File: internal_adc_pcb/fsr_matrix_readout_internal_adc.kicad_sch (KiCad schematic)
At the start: 2 parts

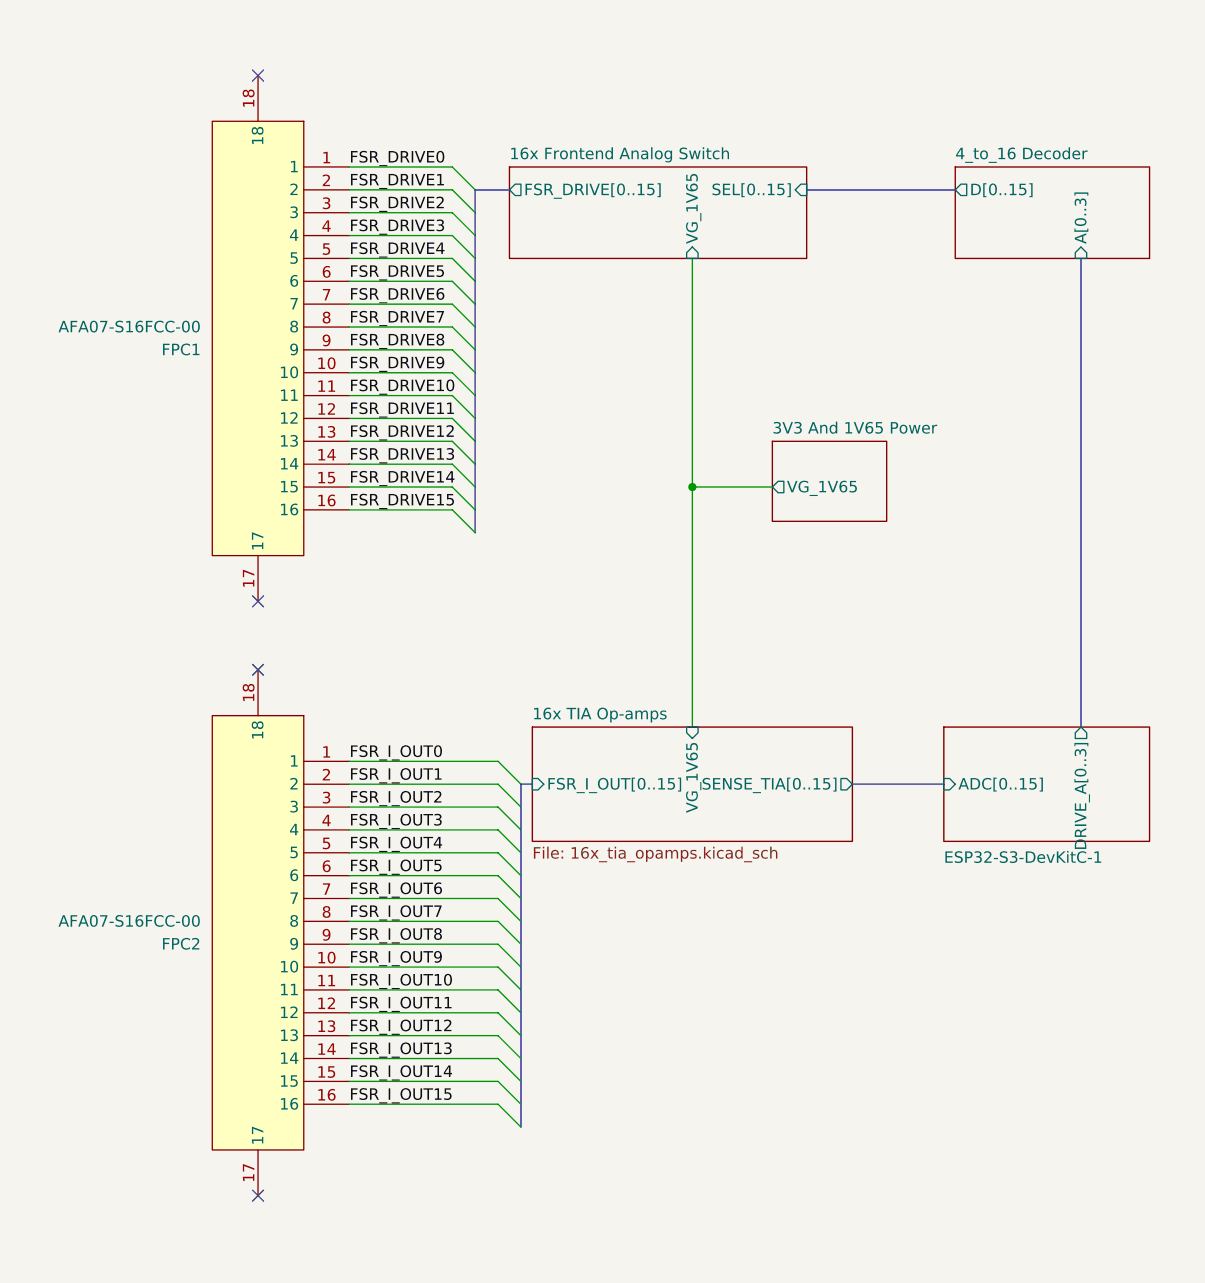
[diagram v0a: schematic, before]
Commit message: adjust VG issue for internal ADC version; changed naming for VG
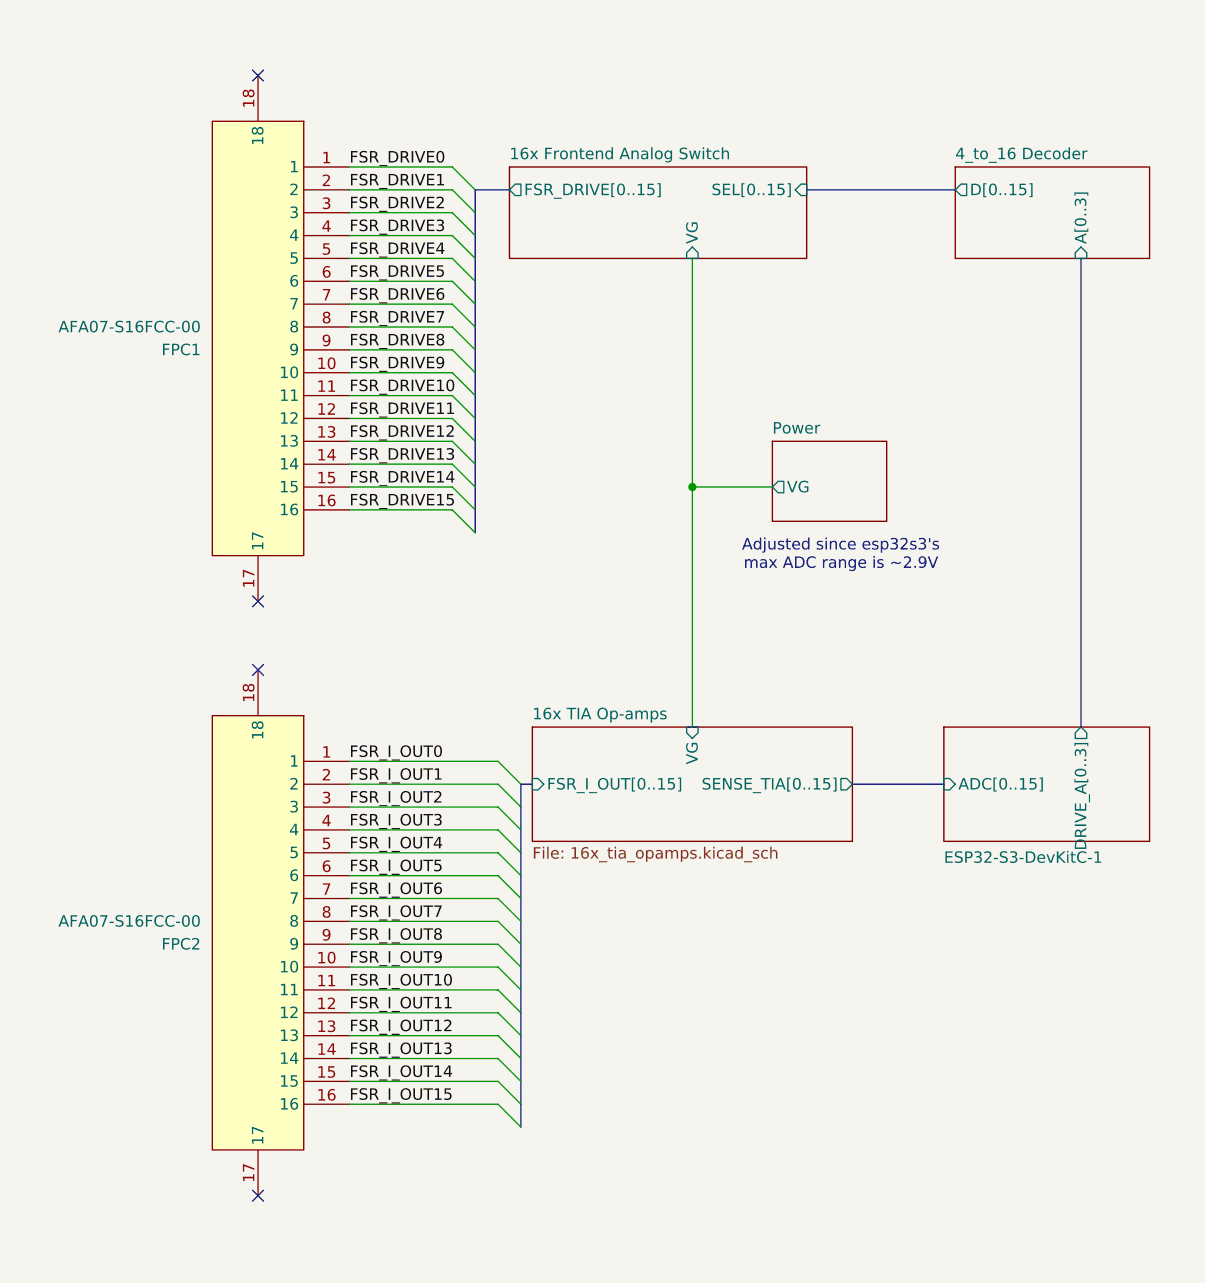
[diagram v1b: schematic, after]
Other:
- sheet 3V3 And 1V65 Power renamed Power
- sheet 16x Frontend Analog Switch ports: added VG; removed VG_1V65
- sheet 16x TIA Op-amps ports: added VG; removed VG_1V65
- sheet Power: file 3V3 And 1V65 Power.kicad_sch -> power.kicad_sch
- sheet Power ports: added VG; removed VG_1V65
- note added: "Adjusted since esp32s3's max ADC range is ~2.9V"
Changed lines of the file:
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@@
 	(generator_version "10.0")
 	(paper "A4")
+	(text "Adjusted since esp32s3's \nmax ADC range is ~2.9V"
+		(exclude_from_sim no)
+		(at 121.92 93.98 0)
+		(effects
+			(font
+				(size 1.27 1.27)
+			)
+		)
+	)
 	(junction
 		(at 105.41 86.36)
@@
 		(members "7bcd2658-0b6a-4321-9860-384b8d346995")
 	)
-	(group "3V3 And 1V65 Power"
-		(lib_id "FSR_readout:3V3 And 1V65 Power")
+	(group "Power"
+		(lib_id "FSR_readout:Power")
 		(members "fdc75ebc-7ada-4013-b8f9-952e82a3d457")
 	)
@@
 			)
 		)
-		(pin "VG_1V65" input
+		(pin "VG" input
 			(at 105.41 60.96 270)
 			(effects
@@
 			)
 		)
-		(pin "VG_1V65" input
+		(pin "VG" input
 			(at 105.41 113.03 90)
 			(effects
@@
 			(color 0 0 0 0)
 		)
-		(property "Sheetname" "3V3 And 1V65 Power"
+		(property "Sheetname" "Power"
 			(at 114.3 80.5684 0)
 			(show_name no)
@@
 			)
 		)
-		(property "Sheetfile" "3V3 And 1V65 Power.kicad_sch"
+		(property "Sheetfile" "power.kicad_sch"
 			(at 114.3 90.7546 0)
 			(hide yes)
@@
 			)
 		)
-		(pin "VG_1V65" output
+		(pin "VG" output
 			(at 114.3 86.36 180)
 			(effects

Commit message: add testpoint for internal ADC ver
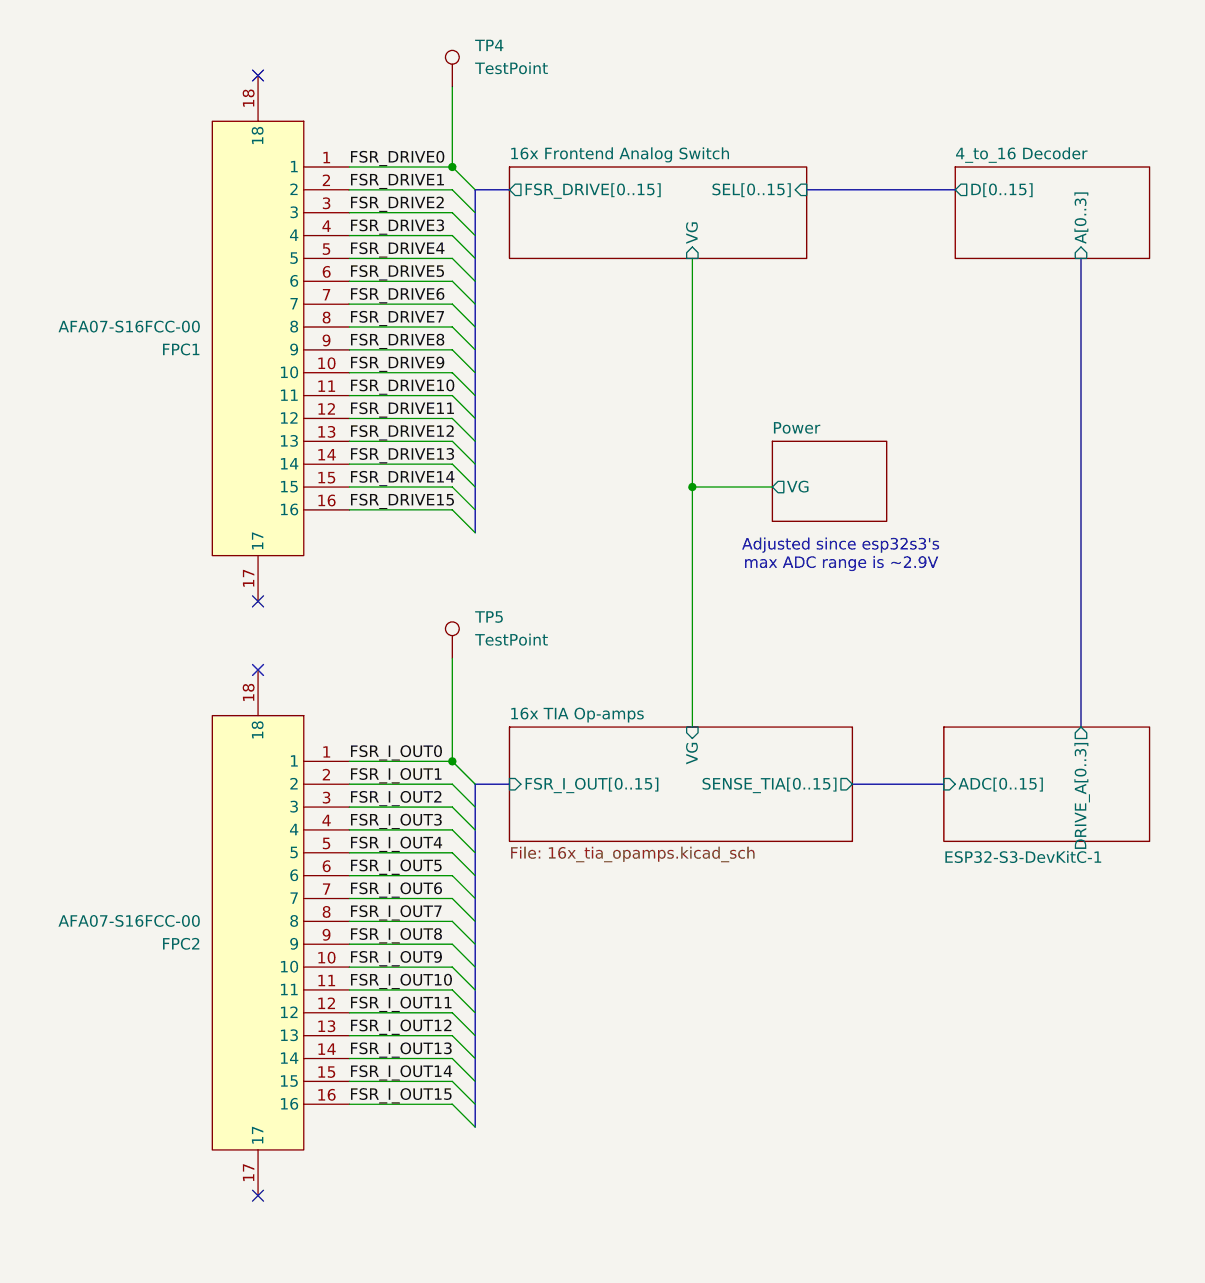
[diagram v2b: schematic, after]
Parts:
- added TP4, TP5: TestPoint, symbol Connector:TestPoint
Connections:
- net FSR_DRIVE0: now also TP4.1
- net FSR_I_OUT0: now also TP5.1

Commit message: update pcb for internal adc version
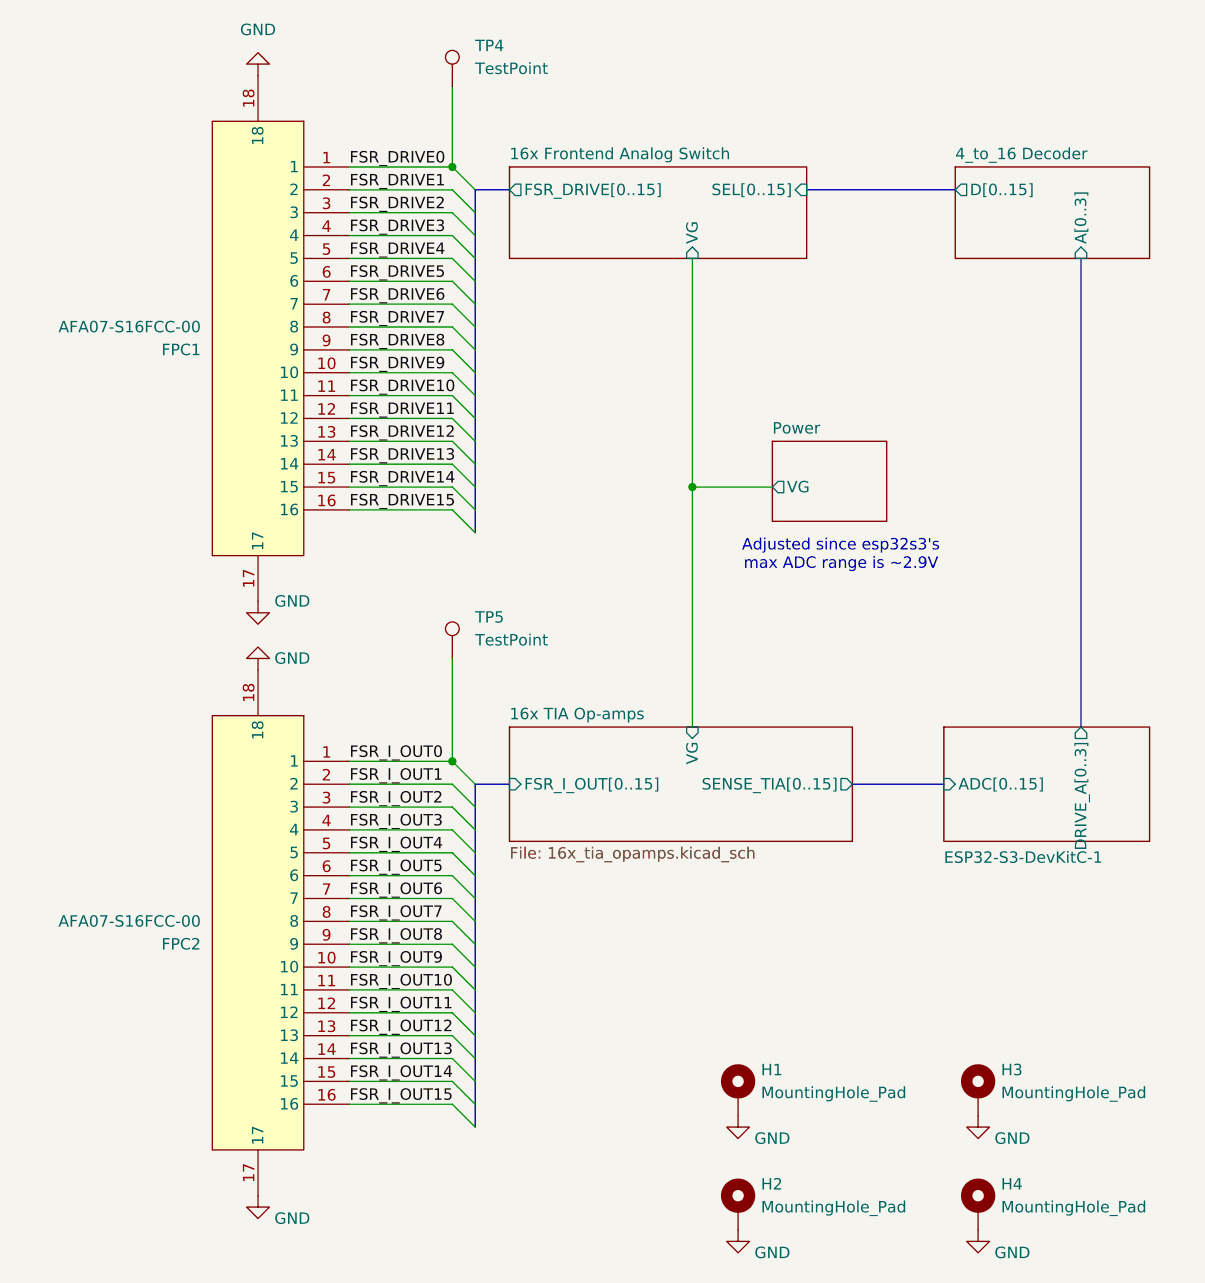
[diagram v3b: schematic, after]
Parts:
- added H1, H2, H3, H4: MountingHole_Pad, MountingHole:MountingHole_2.2mm_M2_DIN965_Pad, symbol Mechanical:MountingHole_Pad
- TP4, TP5: footprint (none) -> TestPoint:TestPoint_Keystone_5000-5004_Miniature
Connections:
- net GND: now reaches FPC2.17
- net GND: now also FPC1.17, FPC1.18, FPC2.18, H1.1, H2.1, H3.1, H4.1
- no-connect marks 4 -> 0

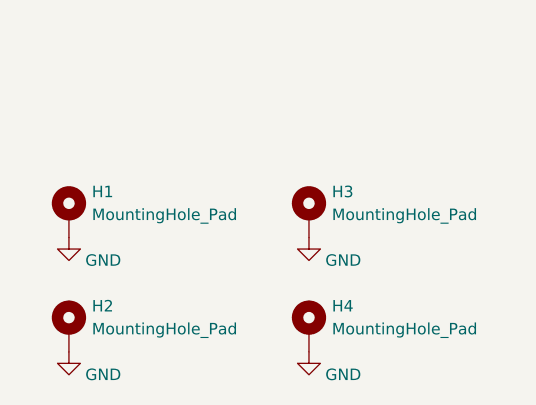
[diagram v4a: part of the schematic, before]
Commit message: fixing all ERC errors for internal ADC ver, fixing warnings now
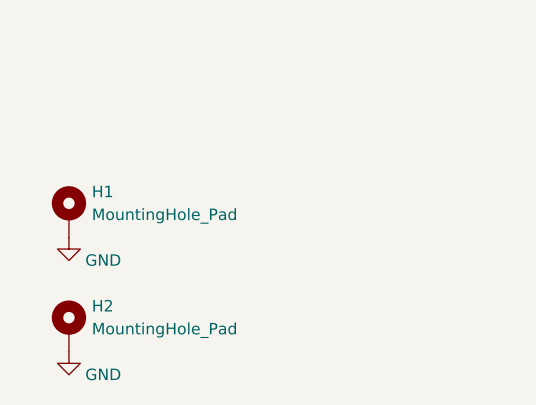
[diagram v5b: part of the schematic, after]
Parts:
- removed H3, H4: MountingHole_Pad, MountingHole:MountingHole_2.2mm_M2_DIN965_Pad, symbol Mechanical:MountingHole_Pad
